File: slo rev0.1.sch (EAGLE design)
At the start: 7 parts, among them IC1 HCTL-1100-44, IC6 A1202LH, IC7 A1202LH, IC8 A1202LH, IC9 A1202LH

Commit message: added  to circuit
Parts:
- removed IC1: HCTL-1100-44, agilent-technologies:HCTL-1100-44
- removed U1: (no value), SparkFun-IC-Special-Function:L6470
- added C1, C2, C3, C4: 0.1uF, resistor:C-USC0603
- added IC2: TB6612FNG, adafruit:TB6612FNG
- added JP2: (no value), adafruit:PINHD-1X8-3.5MM
- added JP3: (no value), adafruit:PINHD-1X6-3.5MM
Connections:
- new net N$1: IC2.AO1, JP2.1
- new net N$10: C1.2, C2.2, C3.2, C4.2, IC6.GND, IC7.GND, IC8.GND, IC9.GND, JP3.6
- new net N$11: IC2.AIN2, JP1.A0
- new net N$12: IC2.AIN1, JP1.A1
- new net N$13: IC2.BIN1, JP1.A2(SPI1_SS)
- new net N$14: IC2.BIN2, JP1.A3(SPI1_SCK)
- new net N$15: IC2.STBY, JP1.D2
- new net N$16: IC2.VM1, IC2.VM2, IC2.VM3
- new net N$18: IC2.PGND1, IC2.PGND1', IC2.PGND2, IC2.PGND2'
- new net N$2: IC2.AO1', JP2.2
- new net N$3: IC2.AO2, JP2.3
- new net N$4: IC2.AO2', JP2.4
- new net N$5: IC2.BO2, JP2.5
- new net N$6: IC2.BO2', JP2.6
- new net N$7: IC2.BO1, JP2.7
- new net N$8: IC2.BO1', JP2.8
- new net N$9: C1.1, C2.1, C3.1, C4.1, IC6.VCC, IC7.VCC, IC8.VCC, IC9.VCC, JP3.1
- new net OUT1: IC6.OUT, JP3.2
- new net OUT2: IC7.OUT, JP3.3
- new net OUT3: IC8.OUT, JP3.4
- new net OUT4: IC9.OUT, JP3.5
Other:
- moved on the sheet: IC6, IC7, IC8, IC9, JP1

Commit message: added more goodies
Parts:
- added C5, C6: (no value), resistor:C-USC1206
- added C7: 2.2uF, clackboard_lib:0603_TANTALUM_CAP
- added C8: 470pF, resistor:C-USC0603
- added CN1: (no value), adafruit:DCBARRELPTH
- added JP4: (no value), adafruit:PINHD-1X6-3.5MM
- added JP5: JUMPER-SMT_2_NO_SILK, SparkFun-Jumpers:JUMPER-SMT_2_NO_SILK
- added JP6: JUMPER-SMT_3_NO_SILK, SparkFun-Jumpers:JUMPER-SMT_3_NO_SILK
- added Q1: 2.5A/30V/105mΩ, SparkFun-DiscreteSemi:MOSFET_PCH-DMG2307L
- added R1: 10K, resistor:R-US_R1206
- added U1: MIC5219 3.3V, SparkFun-IC-Power:V_REG_MIC52193.3V
- JP2: device adafruit:PINHD-1X8-3.5MM -> adafruit:PINHD-1X6-3.5MM
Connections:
- removed net N$16: IC2.VM1, IC2.VM2, IC2.VM3
- removed net N$18: IC2.PGND1, IC2.PGND1', IC2.PGND2, IC2.PGND2'
- removed net N$7: IC2.BO1, JP2.7
- new net GND: C1.2, C2.2, C3.2, C4.2, C5.2, C6.2, C7.-, C8.2, CN1.GND, IC2.GND, IC2.PGND1, IC2.PGND1', IC2.PGND2, IC2.PGND2', IC6.GND, IC7.GND, IC8.GND, IC9.GND, JP1.GND@2, JP1.GND@21, JP2.3, JP2.4, JP3.6, JP4.6, JP6.1, Q1.G, U1.GND
- new net N$17: C8.1, U1.BP
- new net VCC: C1.1, C2.1, C3.1, C4.1, C5.1, C7.+, IC2.VCC, IC6.VCC, IC7.VCC, IC8.VCC, IC9.VCC, JP1.+3V3, JP3.1, JP4.1, R1.2, U1.OUT
- new net VMOTOR: C6.1, IC2.VM1, IC2.VM2, IC2.VM3, JP6.3, Q1.S, U1.IN
- net N$1: now also IC2.AO1'
- net N$10: now also JP1.!RST!; no longer C1.2, C2.2, C3.2, C4.2, IC6.GND, IC7.GND, IC8.GND, IC9.GND, JP3.6
- net N$15: now also JP5.2; no longer IC2.STBY
- net N$2: now also IC2.AO2, IC2.AO2'; no longer IC2.AO1'
- net N$3: now also IC2.BO2, IC2.BO2', JP2.5; no longer IC2.AO2, JP2.3
- net N$4: now also IC2.BO1, IC2.BO1', JP2.6; no longer IC2.AO2', JP2.4
- net N$5: now also CN1.PWR, Q1.D; no longer IC2.BO2, JP2.5
- net N$6: now also IC2.STBY, JP5.1, R1.1; no longer IC2.BO2', JP2.6
- net N$8: now also JP1.VBAT; no longer IC2.BO1', JP2.8
- net N$9: now also JP6.2, U1.EN; no longer C1.1, C2.1, C3.1, C4.1, IC6.VCC, IC7.VCC, IC8.VCC, IC9.VCC, JP3.1
- net OUT1: now also JP1.(JTAG_TCK)D6, JP4.2
- net OUT2: now also JP1.(JTAG_TDI)D5, JP4.3
- net OUT3: now also JP1.(JTAG_TDO)D4, JP4.4
- net OUT4: now also JP1.(JTAG_TRST)D3, JP4.5
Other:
- note added: "12V input"
- moved on the sheet: C1, C2, C3, C4, IC6, IC7, IC8, IC9

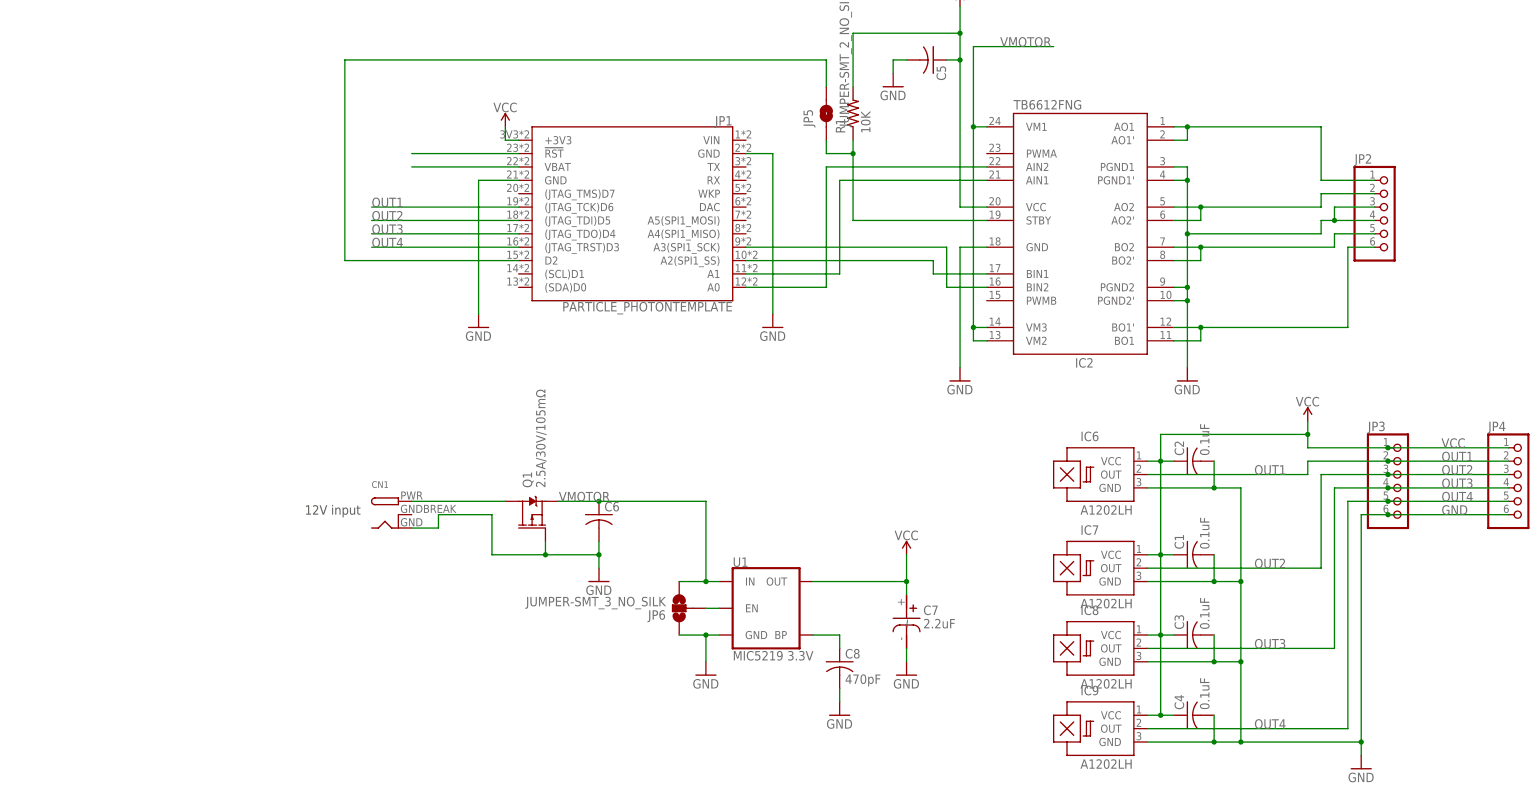
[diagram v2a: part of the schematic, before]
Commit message: removed a hall sensor
need to create option to house an encoder
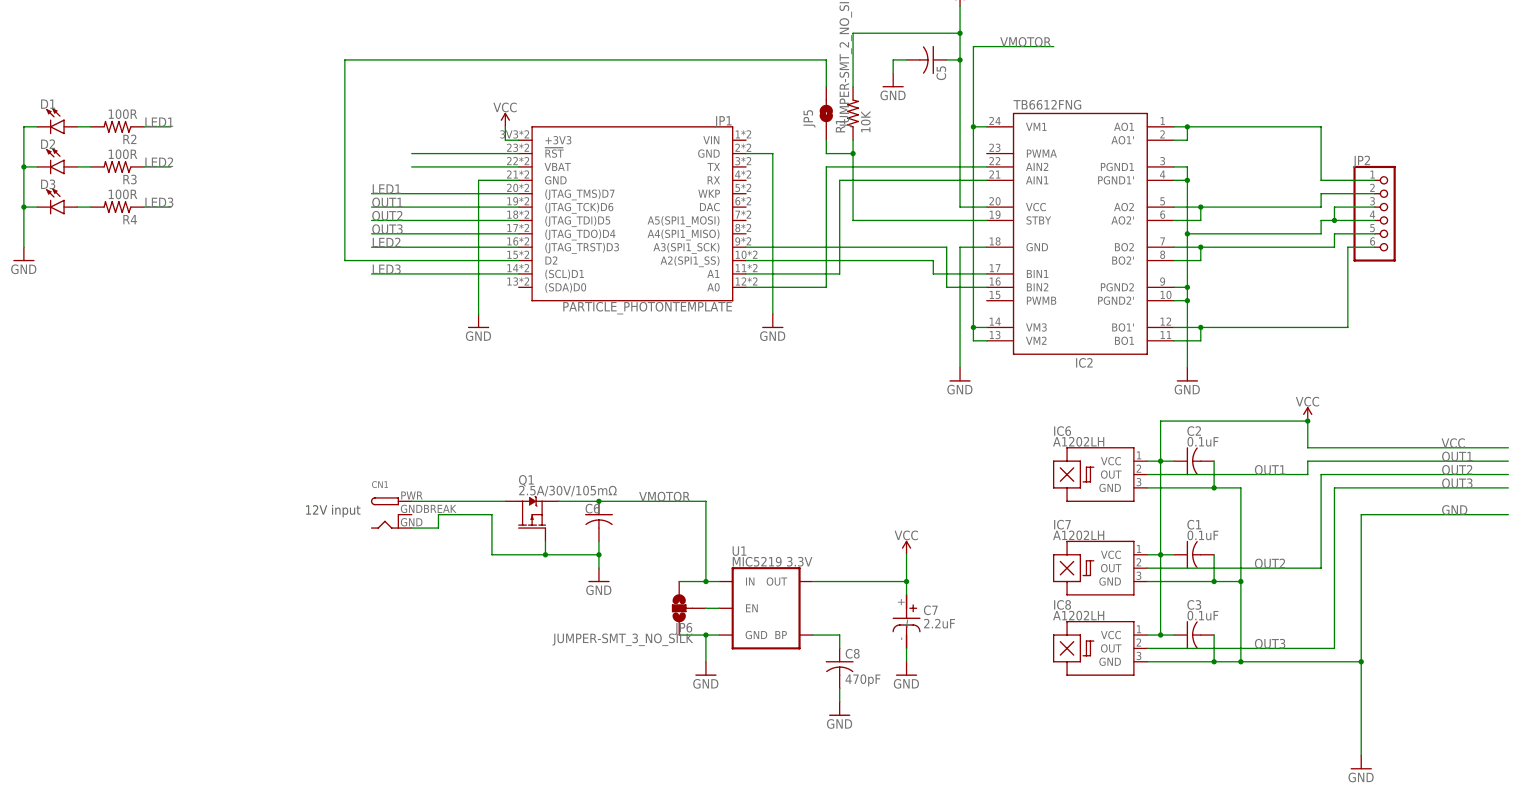
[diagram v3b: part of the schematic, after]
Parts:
- removed C4: 0.1uF, resistor:C-USC0603
- removed IC9: A1202LH, allegro:A1202LH
- removed JP3, JP4: (no value), adafruit:PINHD-1X6-3.5MM
- added D1, D2, D3: (no value), SparkFun-LED:LED-FKIT-1206
- added R2, R3, R4: 100R, resistor:R-US_R1206
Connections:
- removed net OUT4: IC9.OUT, JP1.(JTAG_TRST)D3, JP3.5, JP4.5
- new net LED1: JP1.(JTAG_TMS)D7, R2.1
- new net LED2: JP1.(JTAG_TRST)D3, R3.1
- new net LED3: JP1.(SCL)D1, R4.1
- new net N$16: D2.A, R3.2
- new net N$18: D3.A, R4.2
- new net N$7: D1.A, R2.2
- net GND: now also D1.C, D2.C, D3.C; no longer C4.2, IC9.GND, JP3.6, JP4.6
- net OUT1: no longer JP3.2, JP4.2
- net OUT2: no longer JP3.3, JP4.3
- net OUT3: no longer JP3.4, JP4.4
- net VCC: no longer C4.1, IC9.VCC, JP3.1, JP4.1
